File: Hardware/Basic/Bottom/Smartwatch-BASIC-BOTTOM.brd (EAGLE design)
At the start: 33 x 33 mm, 35 parts, among them U1 AD5242-SO16, U3 PCF8523

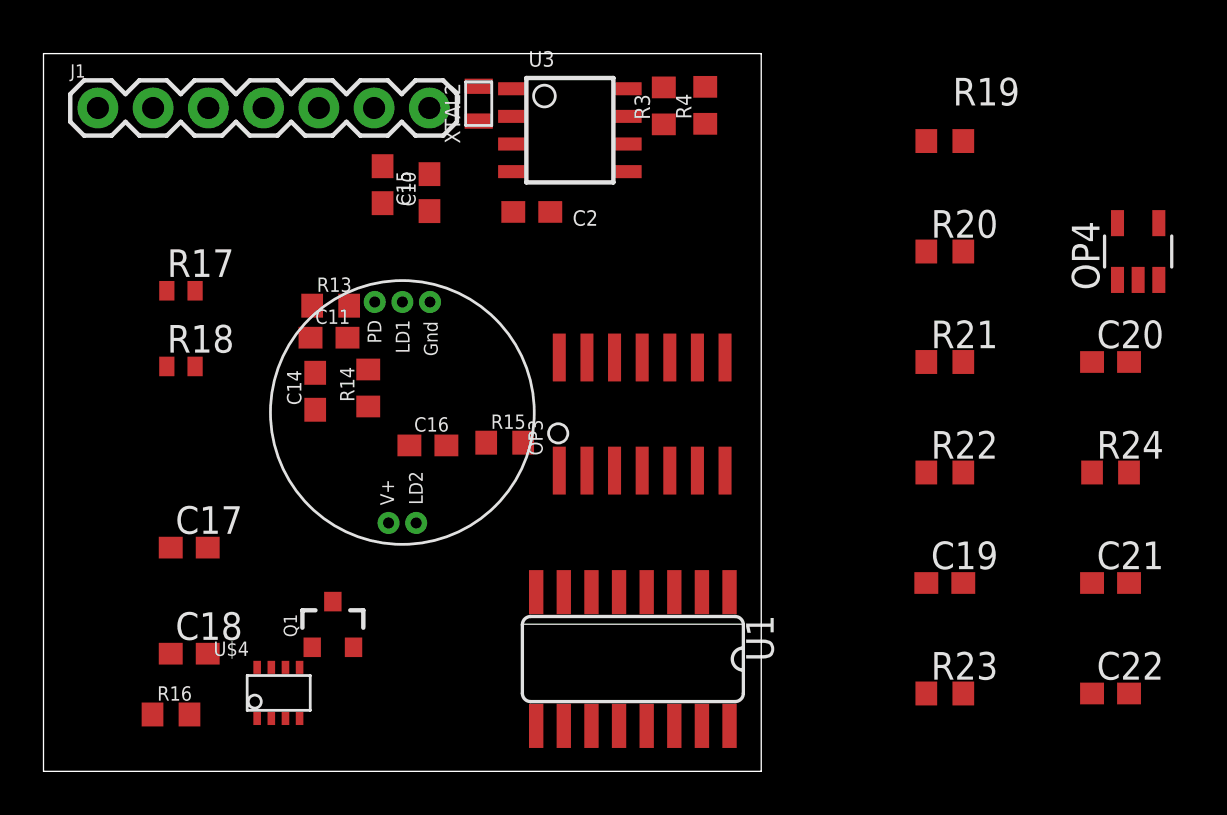
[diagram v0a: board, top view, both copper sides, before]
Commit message: Bottom board routed
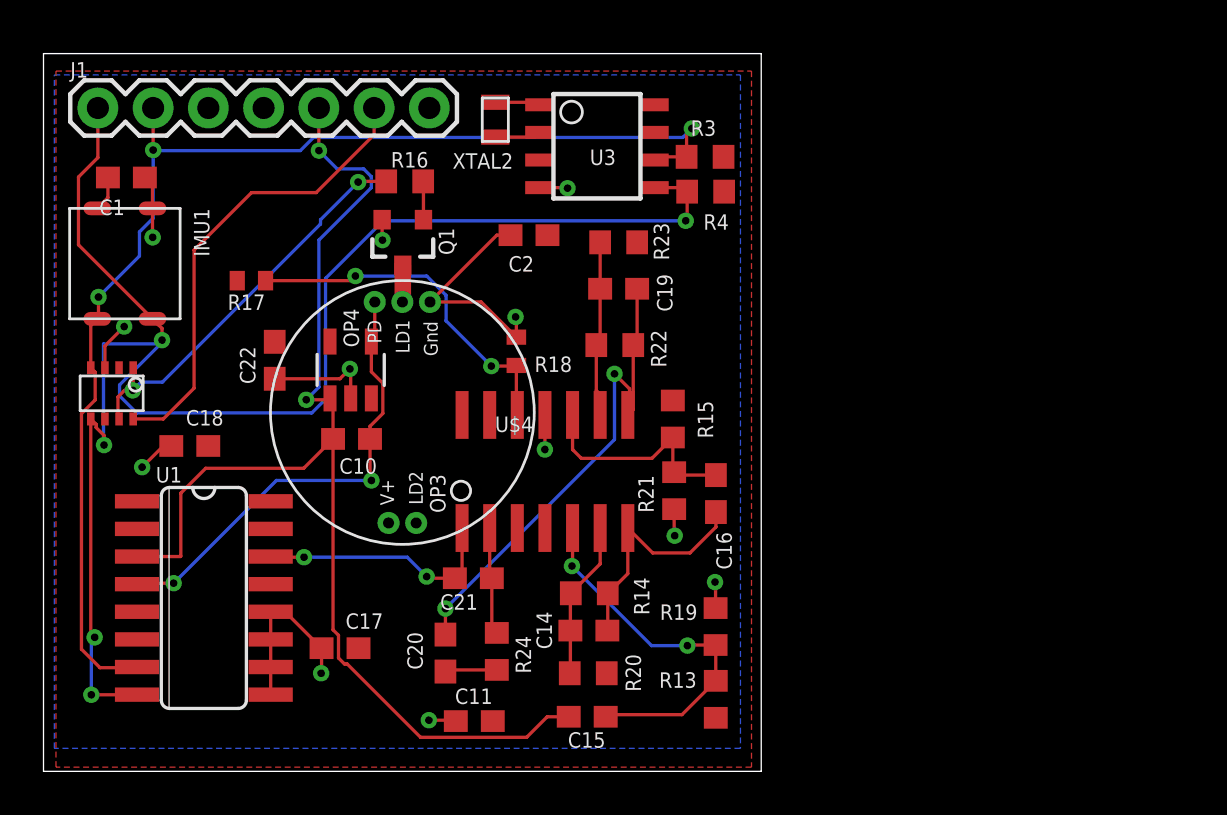
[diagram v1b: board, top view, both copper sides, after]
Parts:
- added C1: 100n, LinnesLab-Passives:C0603
- added IMU1: LSM6DS3_CAST, LinnesLab-Sensors:LSM6DS3_CAST
- moved C22 41.4 mm to (13.1, 21.4), turned to 90 degrees
- moved OP4 36.6 mm to (16.6, 21.0)
- moved C20 33.4 mm to (21.0, 7.94), turned to 270 degrees
- moved R24 29.4 mm to (23.3, 8.01), turned to 270 degrees
- moved C21 29.3 mm to (22.3, 11.4), turned to 180 degrees
- moved R16 26.8 mm to (19.1, 29.6)
- moved C15 26.2 mm to (27.5, 5.01), turned to 0 degrees
- moved R23 25.6 mm to (28.9, 26.8), turned to 180 degrees
- moved R20 25.4 mm to (27.5, 7.01), turned to 180 degrees
- moved R13 25.3 mm to (33.4, 5.81), turned to 270 degrees
- moved R19 24.7 mm to (33.4, 9.16), turned to 270 degrees
- moved C19 20.2 mm to (28.9, 24.7), turned to 180 degrees
- moved U1 19.9 mm to (9.87, 10.5), turned to 270 degrees
- moved C11 18.9 mm to (22.3, 4.81)
- moved Q1 17.9 mm to (19.0, 26.9), turned to 180 degrees
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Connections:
- removed net LED: Q1.3
- removed net LED.CTRL: U$4.8
- removed net TIA: C10.2, C15.1, OP4.1, U1.3
- new net A6/TIA: C10.2, C15.1, J1.5, OP4.1, U1.3
- new net A7/PPG: J1.7
- new net D26/LED.CTRL: J1.6, U$4.8
- net 3.3V: now also C1.2, IMU1.2, J1.4
- net GND: now also C1.1, IMU1.1, J1.3
- net LED.C: now also Q1.3
- net SCL: now also IMU1.3, J1.2
- net SDA: now also IMU1.4, J1.1
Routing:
- net SDA: track 0.00 -> 76.5 mm, vias 0 -> 5
- net SCL: track 0.00 -> 56.6 mm, vias 0 -> 3
- net A6/TIA: track 0.00 -> 55.0 mm, vias 0 -> 2
- net GND: track 0.00 -> 38.1 mm, vias 0 -> 12
- net N$19: track 0.00 -> 23.5 mm, vias 0 -> 2
- net PD.C: track 0.00 -> 21.5 mm, vias 0 -> 2
- net D26/LED.CTRL: track 0.00 -> 21.4 mm
- net N$9: track 0.00 -> 18.6 mm, vias 0 -> 2
- net N$13: track 0.00 -> 17.3 mm, vias 0 -> 2
- net N$10: track 0.00 -> 16.3 mm, vias 0 -> 2
- net PPG: track 0.00 -> 11.3 mm, vias 0 -> 2
- net N$16: track 0.00 -> 10.8 mm
- net N$17: track 0.00 -> 10.4 mm
- net N$15: track 0.00 -> 7.25 mm
- net N$18: track 0.00 -> 7.10 mm
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- added copper zone on layer 1, net 3.3V
- added copper zone on layer 16, net GND

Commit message: Bottom board routed
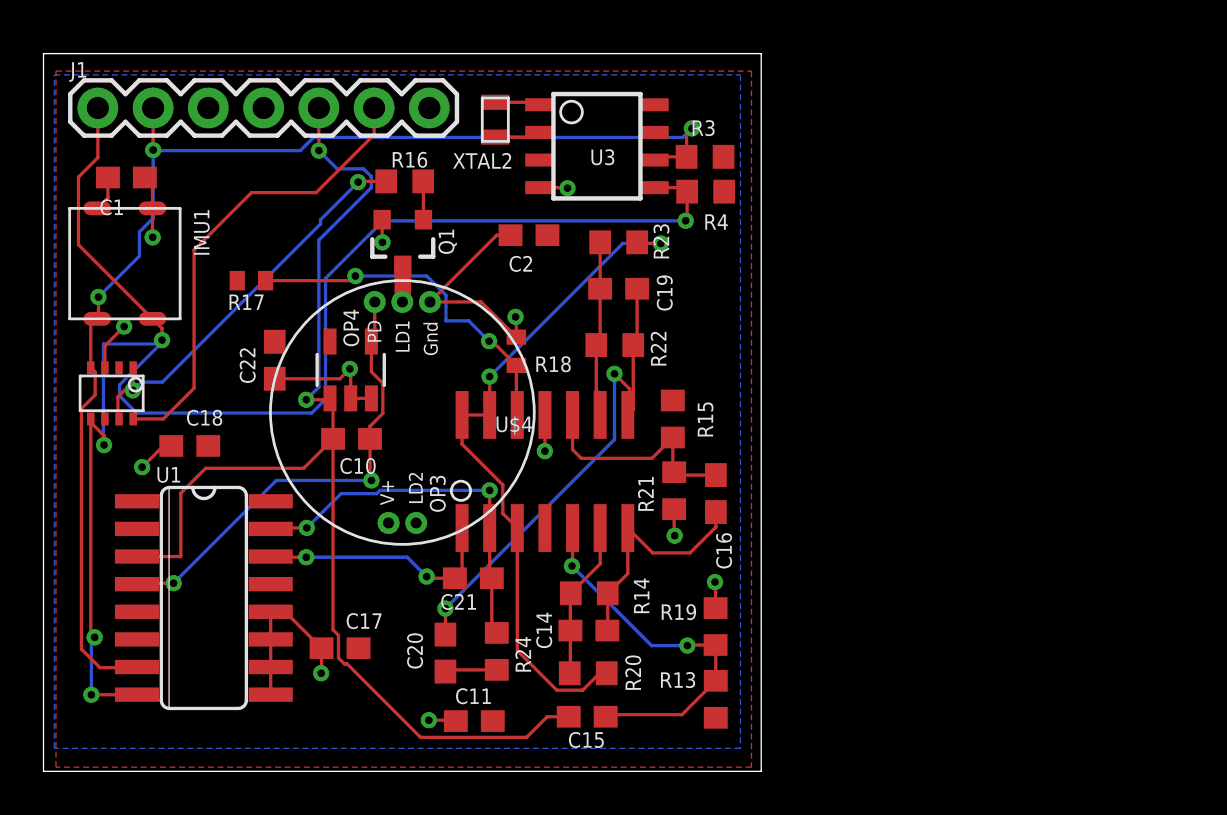
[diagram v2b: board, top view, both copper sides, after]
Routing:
- net VREF: track 0.00 -> 31.6 mm, vias 0 -> 2
- net G.W2: track 4.96 -> 16.7 mm, vias 0 -> 2
- net GND: track 38.1 -> 39.3 mm

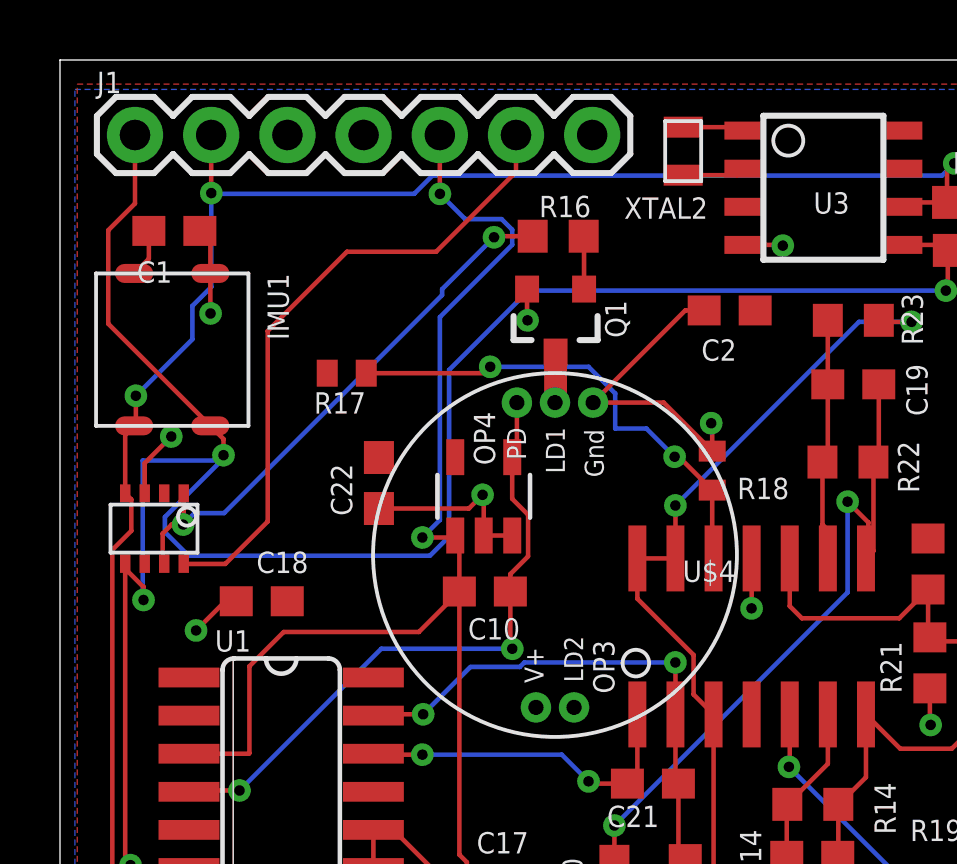
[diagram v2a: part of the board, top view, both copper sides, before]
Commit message: Rearranging Top Board
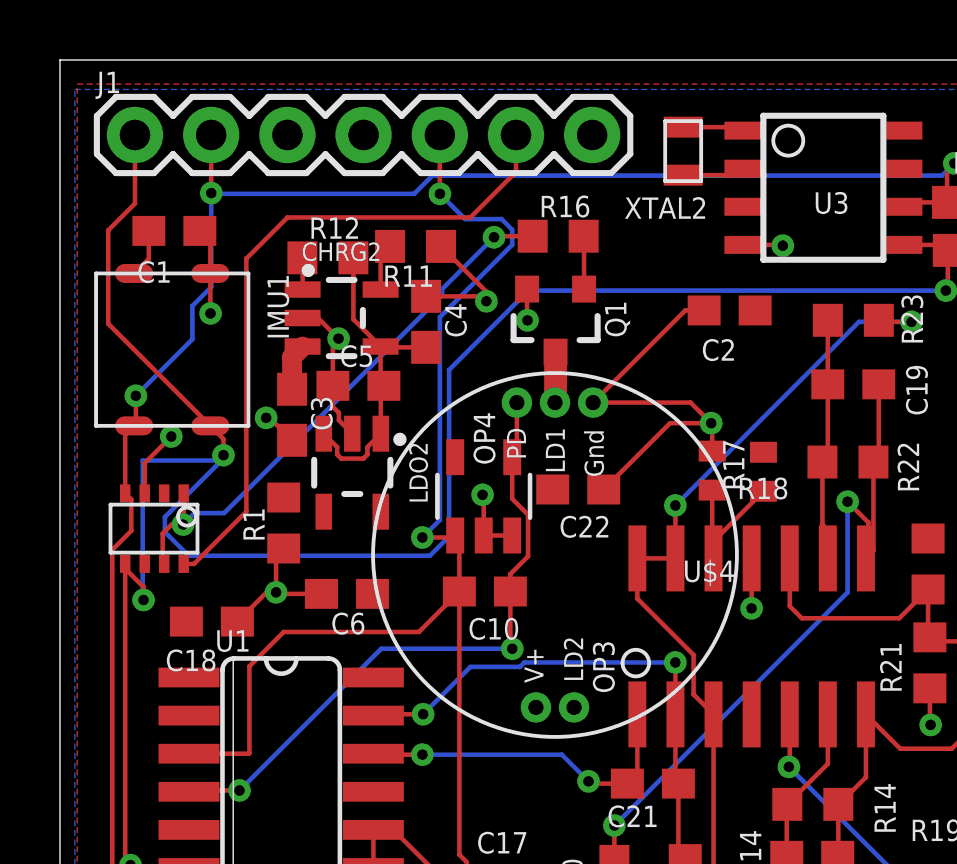
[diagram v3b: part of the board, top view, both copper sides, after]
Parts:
- added C3, C4: 4.7u, LinnesLab-Passives:C0603
- added C5, C6: 1u, LinnesLab-Passives:C0603
- added CHRG2: MCP73831, LinnesLab-Power:SOT23-5
- added LDO2: MIC5504, LinnesLab-Power:SOT23-5
- added R1, R12: 100k, LinnesLab-Passives:R0603
- added R11: (no value), LinnesLab-Passives:R0603
- moved R17 14.3 mm to (25.9, 21.8), turned to 90 degrees
- moved C22 6.65 mm to (19.8, 21.2), turned to 180 degrees
- moved C18 1.80 mm to (7.56, 16.8), turned to 180 degrees
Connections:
- new net D27/CHRG.STAT: CHRG2.1, R12.1
- new net N$1: CHRG2.5, R11.2
- new net VIN1: C4.2, C5.2, CHRG2.4, LDO2.1, LDO2.3, R12.2
- new net VLIPO: C3.1, CHRG2.3
- net 3.3V: now also C6.1, LDO2.5, R1.2
- net GND: now also C3.2, C4.1, C5.1, C6.2, CHRG2.2, LDO2.2, R1.1, R11.1
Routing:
- net GND: track 39.3 -> 53.5 mm, vias 12 -> 15
- net N$10: track 16.3 -> 5.22 mm, vias 2 -> 0
- net VIN1: track 0.00 -> 10.7 mm
- net VLIPO: track 0.00 -> 1.57 mm
- net N$1: track 0.00 -> 1.57 mm
- net D26/LED.CTRL: track 21.4 -> 22.7 mm
- net D27/CHRG.STAT: track 0.00 -> 1.06 mm

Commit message: Rearranged Top Board
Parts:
- removed C3, C4: 4.7u, LinnesLab-Passives:C0603
- removed C5, C6: 1u, LinnesLab-Passives:C0603
- removed CHRG2: MCP73831, LinnesLab-Power:SOT23-5
- removed LDO2: MIC5504, LinnesLab-Power:SOT23-5
- removed R1, R12: 100k, LinnesLab-Passives:R0603
- removed R11: (no value), LinnesLab-Passives:R0603
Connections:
- removed net D27/CHRG.STAT: CHRG2.1, R12.1
- removed net N$1: CHRG2.5, R11.2
- removed net VIN1: C4.2, C5.2, CHRG2.4, LDO2.1, LDO2.3, R12.2
- removed net VLIPO: C3.1, CHRG2.3
- net 3.3V: no longer C6.1, LDO2.5, R1.2
- net GND: no longer C3.2, C4.1, C5.1, C6.2, CHRG2.2, LDO2.2, R1.1, R11.1
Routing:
- net GND: track 53.5 -> 40.9 mm, vias 15 -> 12
- net VIN1: track 10.7 -> 0.00 mm
- net VLIPO: track 1.57 -> 0.00 mm
- net N$1: track 1.57 -> 0.00 mm
- net D27/CHRG.STAT: track 1.06 -> 0.00 mm
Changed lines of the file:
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@@
 <attribute name="VALUE" x="6.9464" y="31.7084" size="0.6604" layer="27" rot="R180"/>
-</element>
-<element name="CHRG2" library="LinnesLab-Power" package="SOT23-5" value="MCP73831" x="11.8872" y="26.8986" smashed="yes" rot="R270">
-<attribute name="NAME" x="11.8872" y="28.8036" size="0.6096" layer="25" ratio="20" align="bottom-center"/>
-<attribute name="PROD_ID" value="IC-09995" x="12.2936" y="26.8986" size="1.778" layer="27" rot="R270" display="off"/>
-<attribute name="VALUE" x="11.8872" y="24.3586" size="0.6096" layer="27" ratio="20" align="bottom-center"/>
-</element>
-<element name="LDO2" library="LinnesLab-Power" package="SOT23-5" value="MIC5504" x="12.2428" y="21.7424" smashed="yes" rot="R180">
-<attribute name="NAME" x="14.1478" y="21.7424" size="0.6096" layer="25" ratio="20" rot="R270" align="bottom-center"/>
-<attribute name="VALUE" x="9.7028" y="21.7424" size="0.6096" layer="27" ratio="20" rot="R270" align="bottom-center"/>
-</element>
-<element name="C5" library="LinnesLab-Passives" package="C0603" package3d_urn="urn:adsk.eagle:package:15661989/2" value="1u" x="12.446" y="24.638" smashed="yes">
-<attribute name="NAME" x="11.811" y="25.273" size="0.7112" layer="25"/>
-<attribute name="VALUE" x="11.811" y="22.733" size="0.7112" layer="27"/>
-</element>
-<element name="C6" library="LinnesLab-Passives" package="C0603" package3d_urn="urn:adsk.eagle:package:15661989/2" value="1u" x="12.065" y="17.7038" smashed="yes" rot="R180">
-<attribute name="NAME" x="12.7" y="17.0688" size="0.7112" layer="25" rot="R180"/>
-<attribute name="VALUE" x="12.7" y="19.6088" size="0.7112" layer="27" rot="R180"/>
-</element>
-<element name="C3" library="LinnesLab-Passives" package="C0603" package3d_urn="urn:adsk.eagle:package:15661989/2" value="4.7u" x="10.2362" y="23.6728" smashed="yes" rot="R270">
-<attribute name="NAME" x="10.8712" y="24.3078" size="0.7112" layer="25" rot="R270"/>
-<attribute name="VALUE" x="8.3312" y="24.3078" size="0.7112" layer="27" rot="R270"/>
-</element>
-<element name="C4" library="LinnesLab-Passives" package="C0603" package3d_urn="urn:adsk.eagle:package:15661989/2" value="4.7u" x="14.7066" y="26.7716" smashed="yes" rot="R270">
-<attribute name="NAME" x="15.3416" y="27.4066" size="0.7112" layer="25" rot="R270"/>
-<attribute name="VALUE" x="12.8016" y="27.4066" size="0.7112" layer="27" rot="R270"/>
-</element>
-<element name="R11" library="LinnesLab-Passives" package="R0603" package3d_urn="urn:adsk.eagle:package:15661944/2" value="" x="14.351" y="29.2862" smashed="yes" rot="R180">
-<attribute name="NAME" x="14.986" y="28.6512" size="0.7112" layer="25" rot="R180"/>
-<attribute name="VALUE" x="14.986" y="31.1912" size="0.7112" layer="27" rot="R180"/>
-</element>
-<element name="R12" library="LinnesLab-Passives" package="R0603" package3d_urn="urn:adsk.eagle:package:15661944/2" value="100k" x="11.43" y="28.9052" smashed="yes">
-<attribute name="NAME" x="10.795" y="29.5402" size="0.7112" layer="25"/>
-<attribute name="VALUE" x="10.795" y="27.0002" size="0.7112" layer="27"/>
-</element>
-<element name="R1" library="LinnesLab-Passives" package="R0603" package3d_urn="urn:adsk.eagle:package:15661944/2" value="100k" x="9.9568" y="20.066" smashed="yes" rot="R90">
-<attribute name="NAME" x="9.3218" y="19.431" size="0.7112" layer="25" rot="R90"/>
-<attribute name="VALUE" x="11.8618" y="19.431" size="0.7112" layer="27" rot="R90"/>
 </element>
 </elements>
@@
 <wire x1="12.9464" y1="8.5664" x2="12.9464" y2="9.8034" width="0.1524" layer="1"/>
 <wire x1="12.9464" y1="9.8034" x2="12.9794" y2="9.8364" width="0.1524" layer="1"/>
-<contactref element="C5" pad="1"/>
-<contactref element="LDO2" pad="2"/>
-<contactref element="C6" pad="2"/>
-<contactref element="C3" pad="2"/>
-<contactref element="R11" pad="1"/>
-<contactref element="C4" pad="1"/>
-<contactref element="CHRG2" pad="2"/>
-<contactref element="R1" pad="1"/>
-<wire x1="11.5706" y1="24.6126" x2="11.5765" y2="24.6185" width="0.1524" layer="1"/>
-<wire x1="11.5765" y1="24.6185" x2="11.596" y2="24.638" width="0.1524" layer="1"/>
 <wire x1="23.5196" y1="24.08" x2="24.2062" y2="23.3934" width="0.1524" layer="1"/>
 <wire x1="20.27" y1="24.08" x2="23.5196" y2="24.08" width="0.1524" layer="1"/>
@@
 <wire x1="9.3882" y1="17.7546" x2="9.7028" y2="17.7546" width="0.1524" layer="1"/>
 <via x="9.7028" y="17.7546" extent="1-16" drill="0.35"/>
-<wire x1="9.9568" y1="19.216" x2="9.7028" y2="18.962" width="0.1524" layer="1"/>
 <wire x1="9.7028" y1="18.962" x2="9.7028" y2="17.7546" width="0.1524" layer="1"/>
-<wire x1="11.215" y1="17.7038" x2="9.7536" y2="17.7038" width="0.1524" layer="1"/>
 <wire x1="9.7536" y1="17.7038" x2="9.7028" y2="17.7546" width="0.1524" layer="1"/>
-<wire x1="15.201" y1="29.2862" x2="16.7132" y2="27.774" width="0.1524" layer="1"/>
-<wire x1="16.7132" y1="27.774" x2="16.7132" y2="27.4574" width="0.1524" layer="1"/>
-<via x="16.7132" y="27.4574" extent="1-16" drill="0.35"/>
-<wire x1="14.7066" y1="27.6216" x2="16.549" y2="27.6216" width="0.1524" layer="1"/>
-<wire x1="16.549" y1="27.6216" x2="16.7132" y2="27.4574" width="0.1524" layer="1"/>
-<wire x1="12.2428" y1="23.0425" x2="11.7964" y2="23.4889" width="0.1524" layer="1"/>
-<wire x1="11.7964" y1="23.4889" x2="11.7964" y2="23.7371875" width="0.1524" layer="1"/>
-<wire x1="11.5765" y1="23.9570875" x2="11.5765" y2="24.6185" width="0.1524" layer="1"/>
-<wire x1="11.7964" y1="23.7371875" x2="11.5765" y2="23.9570875" width="0.1524" layer="1"/>
-<wire x1="11.596" y1="24.638" x2="11.596" y2="26.0232" width="0.1524" layer="1"/>
-<wire x1="11.596" y1="26.0232" x2="11.7856" y2="26.2128" width="0.1524" layer="1"/>
-<via x="11.7856" y="26.2128" extent="1-16" drill="0.35"/>
-<wire x1="10.5871" y1="26.8986" x2="11.0998" y2="26.8986" width="0.1524" layer="1"/>
-<wire x1="11.0998" y1="26.8986" x2="11.7856" y2="26.2128" width="0.1524" layer="1"/>
-<wire x1="10.2362" y1="22.8228" x2="9.4878" y2="23.5712" width="0.1524" layer="1"/>
-<wire x1="9.4878" y1="23.5712" x2="9.3726" y2="23.5712" width="0.1524" layer="1"/>
-<via x="9.3726" y="23.5712" extent="1-16" drill="0.35"/>
 </signal>
 <signal name="3.3V">
@@
 <wire x1="5.4614" y1="29.8034" x2="5.4614" y2="28.8744" width="0.1524" layer="1"/>
 <wire x1="5.4614" y1="28.8744" x2="4.9718" y2="28.3848" width="0.1524" layer="1"/>
-<contactref element="LDO2" pad="5"/>
-<contactref element="C6" pad="1"/>
-<contactref element="R1" pad="2"/>
 <wire x1="5.3238" y1="18.7024" x2="6.7136" y2="16.78" width="0" layer="19" extent="1-1"/>
 </signal>
@@
 <wire x1="6.9676" y1="18.7024" x2="6.6238" y2="18.7024" width="0.1524" layer="1"/>
 </signal>
-<signal name="N$1">
-<contactref element="CHRG2" pad="5"/>
-<contactref element="R11" pad="2"/>
-<wire x1="13.1873" y1="27.8486" x2="13.1873" y2="28.9725" width="0.1524" layer="1"/>
-<wire x1="13.1873" y1="28.9725" x2="13.501" y2="29.2862" width="0.1524" layer="1"/>
-</signal>
-<signal name="VLIPO">
-<contactref element="CHRG2" pad="3"/>
-<contactref element="C3" pad="1"/>
-<wire x1="10.2362" y1="24.5228" x2="10.2362" y2="25.5977" width="0.6604" layer="1"/>
-<wire x1="10.2362" y1="25.5977" x2="10.5871" y2="25.9486" width="0.6604" layer="1"/>
-</signal>
-<signal name="D27/CHRG.STAT">
-<contactref element="R12" pad="1"/>
-<contactref element="CHRG2" pad="1"/>
-<wire x1="10.5871" y1="27.8486" x2="10.5871" y2="28.8981" width="0.1524" layer="1"/>
-<wire x1="10.5871" y1="28.8981" x2="10.58" y2="28.9052" width="0.1524" layer="1"/>
-</signal>
-<signal name="VIN1">
-<contactref element="C5" pad="2"/>
-<contactref element="LDO2" pad="1"/>
-<contactref element="LDO2" pad="3"/>
-<contactref element="CHRG2" pad="4"/>
-<contactref element="C4" pad="2"/>
-<contactref element="R12" pad="2"/>
-<wire x1="13.1928" y1="23.0425" x2="13.1928" y2="24.5348" width="0.1524" layer="1"/>
-<wire x1="13.1928" y1="24.5348" x2="13.296" y2="24.638" width="0.1524" layer="1"/>
-<wire x1="12.28" y1="28.9052" x2="12.28" y2="26.8559" width="0.1524" layer="1"/>
-<wire x1="12.28" y1="26.8559" x2="13.1873" y2="25.9486" width="0.1524" layer="1"/>
-<wire x1="13.296" y1="24.638" x2="13.1873" y2="24.7467" width="0.1524" layer="1"/>
-<wire x1="13.1873" y1="24.7467" x2="13.1873" y2="25.9486" width="0.1524" layer="1"/>
-<wire x1="14.7066" y1="25.9216" x2="13.2143" y2="25.9216" width="0.1524" layer="1"/>
-<wire x1="13.2143" y1="25.9216" x2="13.1873" y2="25.9486" width="0.1524" layer="1"/>
-<wire x1="11.2928" y1="23.0425" x2="11.7392" y2="22.5961" width="0.1524" layer="1"/>
-<wire x1="11.7392" y1="22.5961" x2="11.7392" y2="22.3478125" width="0.1524" layer="1"/>
-<wire x1="11.7392" y1="22.3478125" x2="11.8731125" y2="22.2139" width="0.1524" layer="1"/>
-<wire x1="12.6124875" y1="22.2139" x2="12.7464" y2="22.3478125" width="0.1524" layer="1"/>
-<wire x1="12.7464" y1="22.3478125" x2="12.7464" y2="22.5961" width="0.1524" layer="1"/>
-<wire x1="12.7464" y1="22.5961" x2="13.1928" y2="23.0425" width="0.1524" layer="1"/>
-<wire x1="11.8731125" y1="22.2139" x2="12.6124875" y2="22.2139" width="0.1524" layer="1"/>
-</signal>
 </signals>
